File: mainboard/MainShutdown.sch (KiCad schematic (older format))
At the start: 21 parts, among them J10 CONN_2X2, J6 CONN_2X2, K1 KT12-1A, K2 G6DN 12V, Q1 SSM3K361TU,LF, Q2 TSM2312, U13 TS3704IPT, U14 CD4044, U15 CD4082, U4 MainBoard_AD8244

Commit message: docs
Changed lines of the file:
@@
 RESET
-Wire Notes Line
-	4250 7700 4250 5550
 Wire Notes Line
 	4250 5500 600  5500
@@
 Wire Wire Line
 	7300 4350 7950 4350
+Wire Notes Line
+	4250 5500 4250 7700
 $EndSCHEMATC

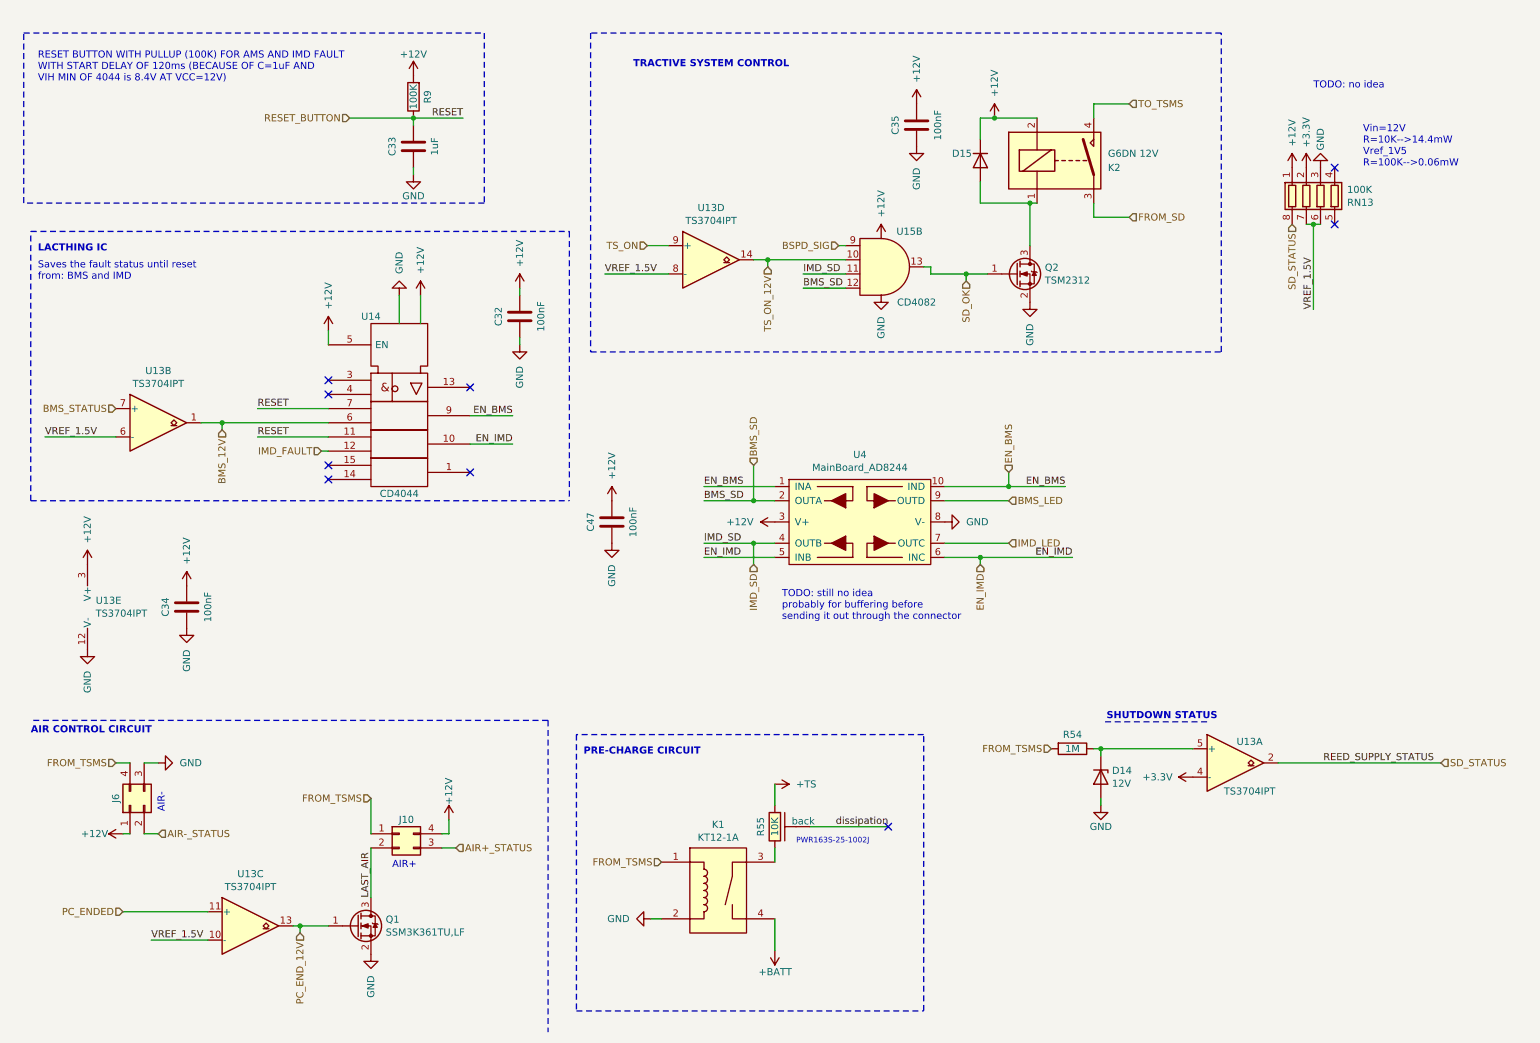
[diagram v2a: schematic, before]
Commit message: 64pin, testpoints, commenting, general refactoring
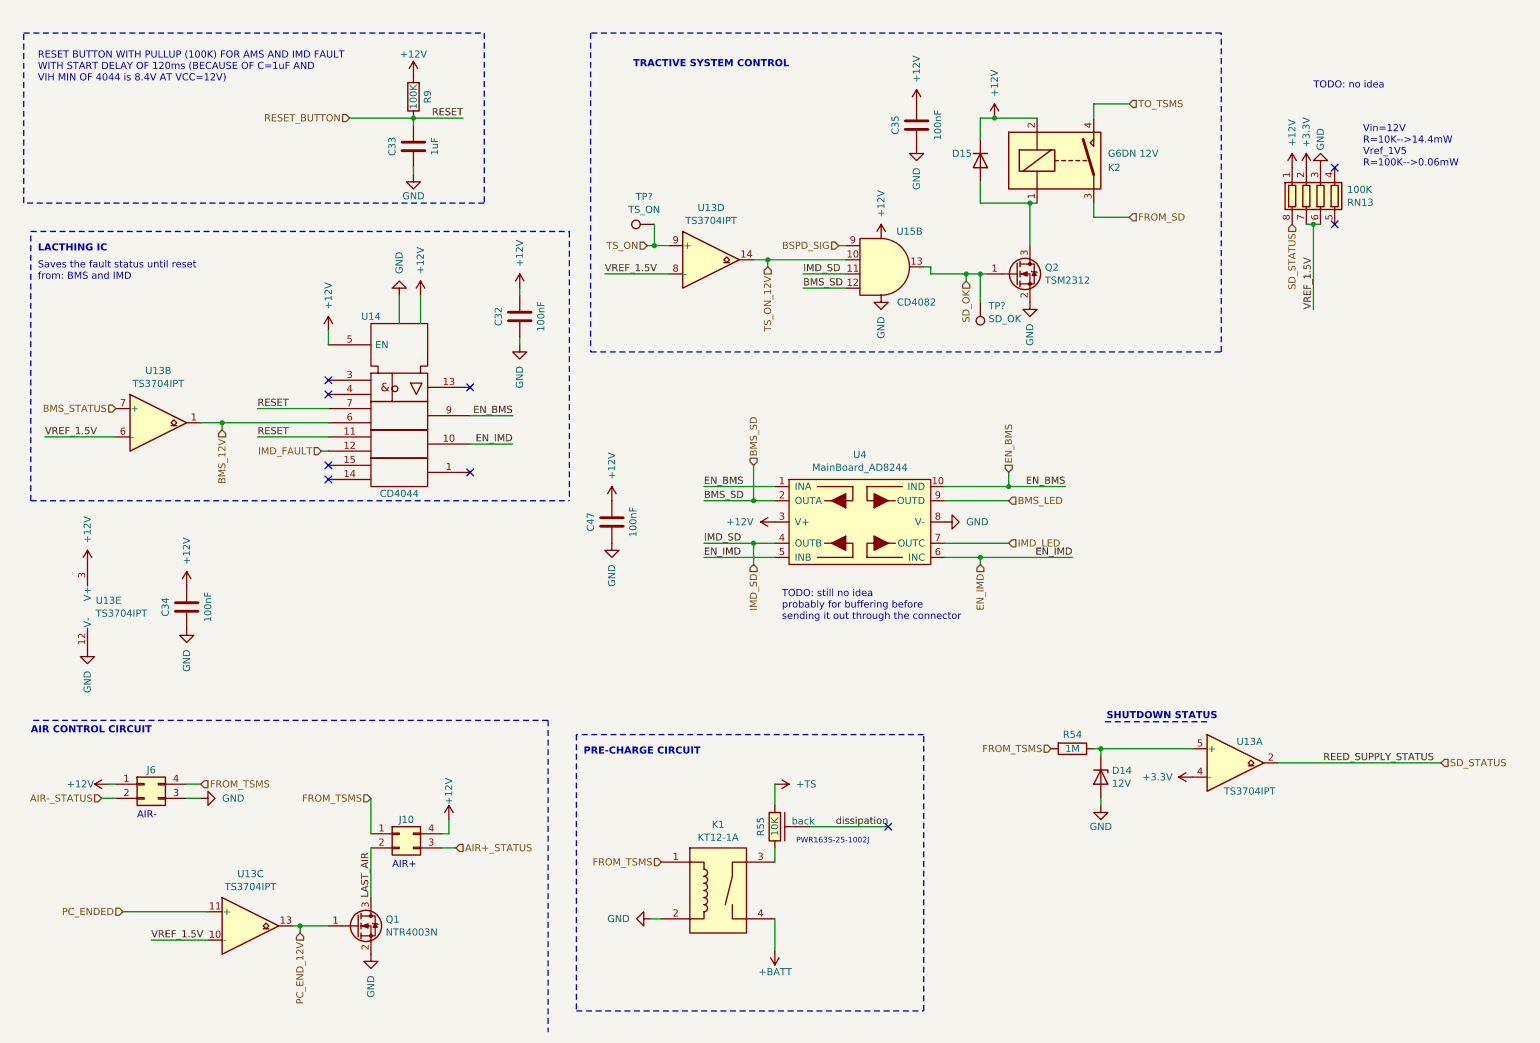
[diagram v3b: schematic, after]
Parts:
- added TP?: SD_OK, symbol Connector:TestPoint
- added TP?: TS_ON, symbol Connector:TestPoint
- Q1: value SSM3K361TU,LF -> NTR4003N; footprint Package_TO_SOT_SMD:SOT-323_SC-70 -> Package_TO_SOT_SMD:SOT-23
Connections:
- net SD_OK: now also TP?.1
- net TS_ON: now also TP?.1
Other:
- moved on the sheet: J6
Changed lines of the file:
@@
 Wire Wire Line
 	3550 6300 3500 6300
-Wire Wire Line
-	1250 6300 1300 6300
 $Comp
 L MainBoard:R_power_backplane R55
@@
 L power:+12V #PWR?
 U 1 1 5E2E4AFA
-P 1250 6300
+P 1150 5950
 AR Path="/5E2E4AFA" Ref="#PWR?"  Part="1"
 AR Path="/5B045B0D/5E2E4AFA" Ref="#PWR0140"  Part="1"
-F 0 "#PWR0140" H 1250 6150 50  0001 C CNN
-F 1 "+12V" V 1250 6500 50  0000 C CNN
-F 2 "" H 1250 6300 50  0001 C CNN
-F 3 "" H 1250 6300 50  0001 C CNN
-	1    1250 6300
+F 0 "#PWR0140" H 1150 5800 50  0001 C CNN
+F 1 "+12V" V 1150 6150 50  0000 C CNN
+F 2 "" H 1150 5950 50  0001 C CNN
+F 3 "" H 1150 5950 50  0001 C CNN
+	1    1150 5950
 	0    -1   -1   0
 $EndComp
 Text HLabel 3600 6400 2    50   Input ~ 0
 AIR+_STATUS
-Text HLabel 1500 6300 2    50   Input ~ 0
+Text HLabel 1100 6050 0    50   Input ~ 0
 AIR-_STATUS
 Text Label 6650 6250 2    50   ~ 0
@@
 L power:GND #PWR0135
 U 1 1 5B0DE170
-P 1500 5800
-F 0 "#PWR0135" H 1500 5550 50  0001 C CNN
-F 1 "GND" V 1500 5650 50  0000 R CNN
-F 2 "" H 1500 5800 50  0001 C CNN
-F 3 "" H 1500 5800 50  0001 C CNN
-	1    1500 5800
+P 1800 6050
+F 0 "#PWR0135" H 1800 5800 50  0001 C CNN
+F 1 "GND" V 1800 5900 50  0000 R CNN
+F 2 "" H 1800 6050 50  0001 C CNN
+F 3 "" H 1800 6050 50  0001 C CNN
+	1    1800 6050
 	0    -1   -1   0
 $EndComp
 Wire Wire Line
-	1300 5800 1200 5800
-Wire Wire Line
-	1500 5800 1400 5800
-Text HLabel 1200 5800 0    50   Input ~ 0
+	1700 5950 1800 5950
+Wire Wire Line
+	1800 6050 1700 6050
+Text HLabel 1800 5950 2    50   Input ~ 0
 FROM_TSMS
 Wire Wire Line
@@
 P 2900 6950
 F 0 "Q1" H 3104 6996 50  0000 L CNN
-F 1 "SSM3K361TU,LF" H 3104 6905 50  0000 L CNN
-F 2 "Package_TO_SOT_SMD:SOT-323_SC-70" H 3100 7050 50  0001 C CNN
+F 1 "NTR4003N" H 3104 6905 50  0000 L CNN
+F 2 "Package_TO_SOT_SMD:SOT-23" H 3100 7050 50  0001 C CNN
 F 3 "https://www.mouser.it/ProductDetail/Toshiba/SSM3K361TULF?qs=sGAEpiMZZMshyDBzk1%2FWi%2FD7Em5shE8qqtsfXGfVhuGHqmGZGu2Z8A%3D%3D" H 2900 6950 50  0001 C CNN
 	1    2900 6950
@@
 	3500 6400 3600 6400
 Wire Wire Line
-	1400 6300 1500 6300
+	1200 6050 1100 6050
 Wire Notes Line
 	3800 650  3800 1850
@@
 L Connector_Generic:Conn_02x02_Counter_Clockwise J?
 U 1 1 5E5D4844
-P 1300 6100
+P 1400 5950
 AR Path="/5B50ED38/5E5D4844" Ref="J?"  Part="1"
 AR Path="/5B045B0D/5E5D4844" Ref="J6"  Part="1"
-F 0 "J6" H 1350 6200 50  0000 C CNN
-F 1 "CONN_2X2" H 1350 6226 50  0001 C CNN
-F 2 "MainBoard:Molex_Micro-Fit_3.0_43045-0412_2x02_P3.00mm_Vertical" H 1300 6100 50  0001 C CNN
-F 3 "~" H 1300 6100 50  0001 C CNN
-	1    1300 6100
-	0    -1   -1   0
+F 0 "J6" H 1450 6050 50  0000 C CNN
+F 1 "CONN_2X2" H 1450 6076 50  0001 C CNN
+F 2 "MainBoard:Molex_Micro-Fit_3.0_43045-0412_2x02_P3.00mm_Vertical" H 1400 5950 50  0001 C CNN
+F 3 "~" H 1400 5950 50  0001 C CNN
+	1    1400 5950
+	1    0    0    -1
 $EndComp
 Wire Wire Line
@@
 Connection ~ 7200 2350
 Wire Wire Line
-	7200 2350 7350 2350
+	7200 2350 7300 2350
 Wire Wire Line
 	6950 2350 7200 2350
@@
 Text Notes 3150 6550 0    50   ~ 0
 AIR+
-Text Notes 1550 6150 1    50   ~ 0
+Text Notes 1350 6200 0    50   ~ 0
 AIR-
 $Comp
@@
 Wire Wire Line
 	4650 2350 5100 2350
-Wire Wire Line
-	4950 2150 5100 2150
 $Comp
 L Comparator:LM339 U13
@@
 Wire Notes Line
 	4250 5500 4250 7700
+$Comp
+L Connector:TestPoint TP?
+U 1 1 6059EB75
+P 7300 2550
+F 0 "TP?" H 7242 2576 50  0000 R CNN
+F 1 "SD_OK" H 7242 2667 50  0000 R CNN
+F 2 "" H 7500 2550 50  0001 C CNN
+F 3 "~" H 7500 2550 50  0001 C CNN
+	1    7300 2550
+	-1   0    0    1
+$EndComp
+Wire Wire Line
+	7300 2550 7300 2350
+Connection ~ 7300 2350
+Wire Wire Line
+	7300 2350 7350 2350
+$Comp
+L Connector:TestPoint TP?
+U 1 1 605A3994
+P 5000 2000
+F 0 "TP?" V 5195 2072 50  0000 C CNN
+F 1 "TS_ON" V 5104 2072 50  0000 C CNN
+F 2 "" H 5200 2000 50  0001 C CNN
+F 3 "~" H 5200 2000 50  0001 C CNN
+	1    5000 2000
+	0    -1   -1   0
+$EndComp
+Wire Wire Line
+	4950 2150 5000 2150
+Wire Wire Line
+	5000 2000 5000 2150
+Connection ~ 5000 2150
+Wire Wire Line
+	5000 2150 5100 2150
+Wire Wire Line
+	1150 5950 1200 5950
 $EndSCHEMATC

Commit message: renamed shutdown nets
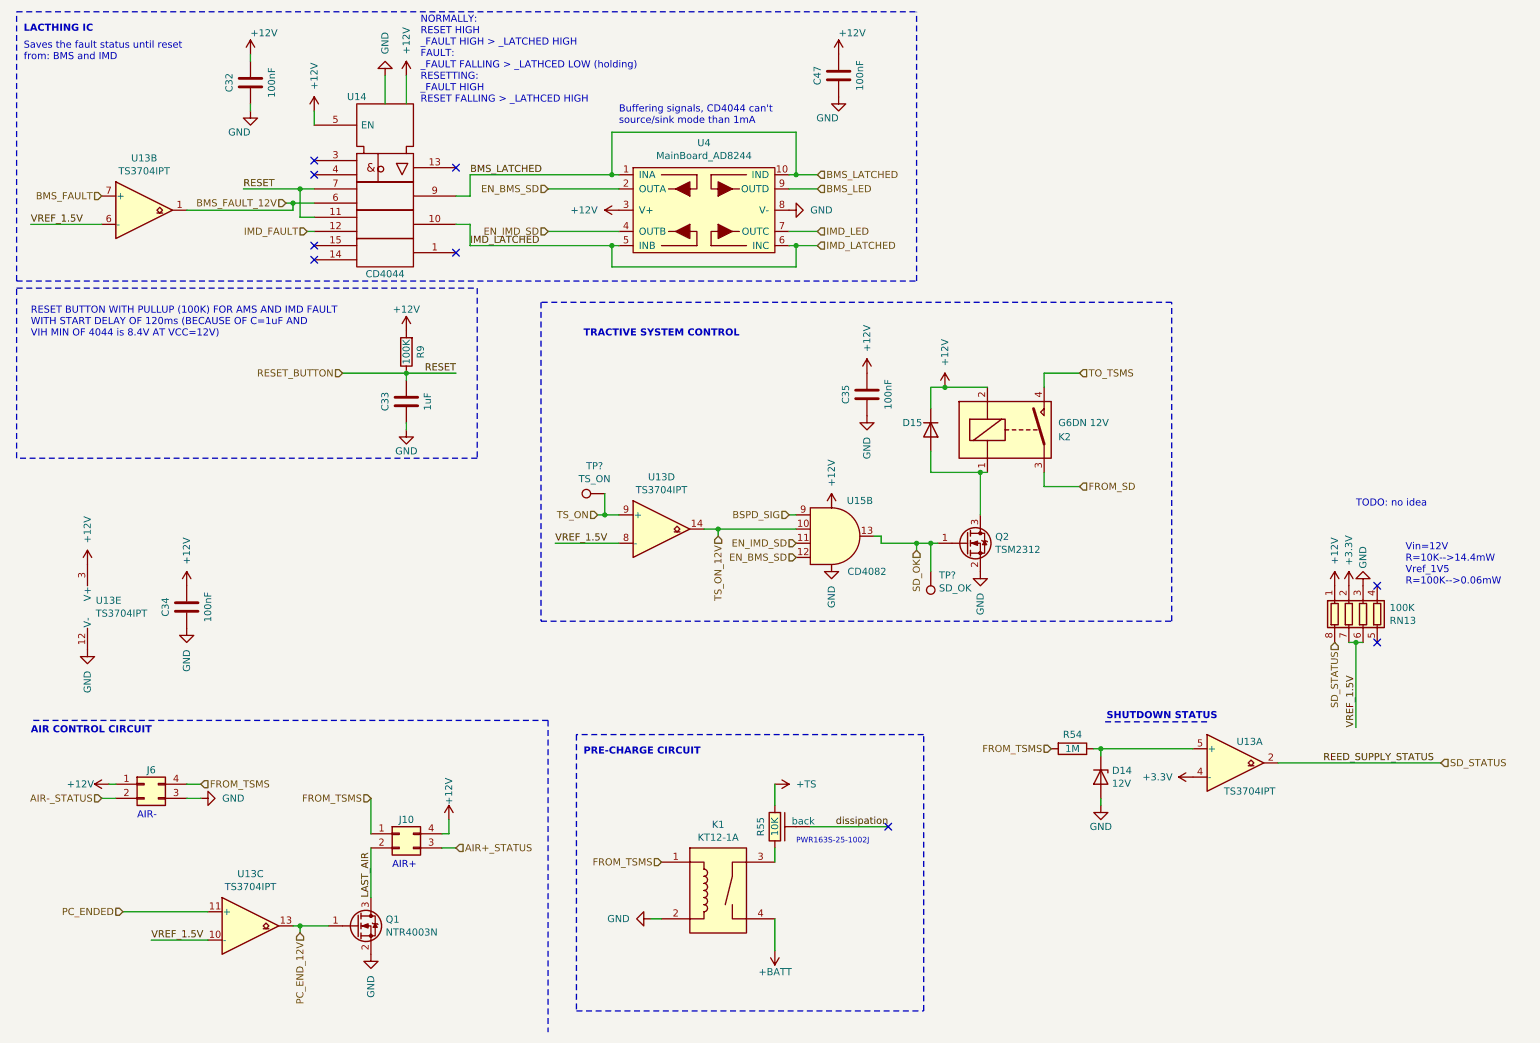
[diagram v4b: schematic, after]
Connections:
- net BMS_12V renamed BMS_FAULT_12V
- net BMS_SD renamed EN_BMS_SD
- net BMS_STATUS renamed BMS_FAULT
- net EN_BMS renamed BMS_LATCHED
- net EN_IMD renamed IMD_LATCHED
- net IMD_SD renamed EN_IMD_SD
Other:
- note added: "Buffering signals, CD4044 can't \nsource/sink mode than 1mA"
- note added: "NORMALLY:\nRESET HIGH\n_FAULT HIGH > _LATCHED HIGH\nFAULT:\n_FAULT FALLING > _LATHCED LOW (holding)\nRESETTING:\n_FAULT HIGH\nRESET FALLING > _LATHCED HIGH"
- note removed: "TODO: still no idea\nprobably for buffering before \nsending it out through the connector\n"
- moved on the sheet: C32, C33, C35, C47, D15, K2, Q2, R9, RN13, TP?, U13B, U13D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
